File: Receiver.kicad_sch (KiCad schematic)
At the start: 21 parts, among them J15 ReceiverRS485, J23 ReceiverData, U17 AMS1117-5.0, U23 MAX485EE

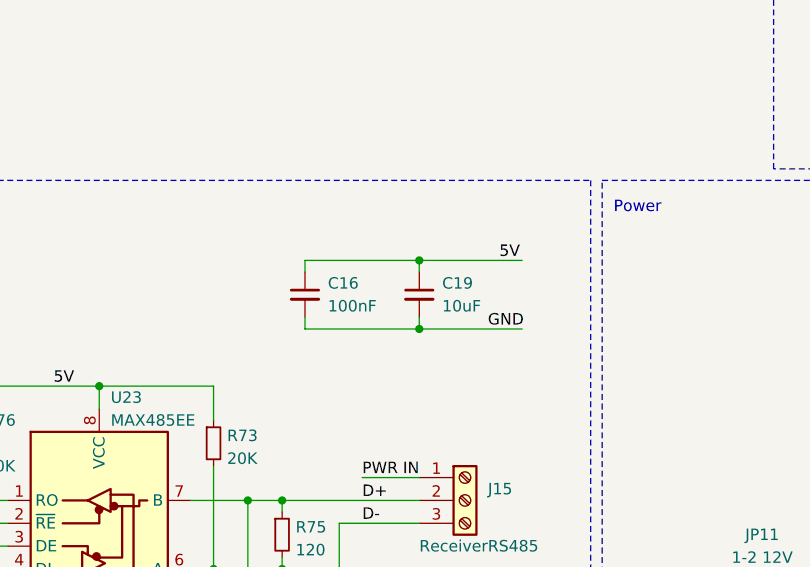
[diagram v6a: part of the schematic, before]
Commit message: fix: DRC & ERC revealed designators were out of sync between schem and pcb
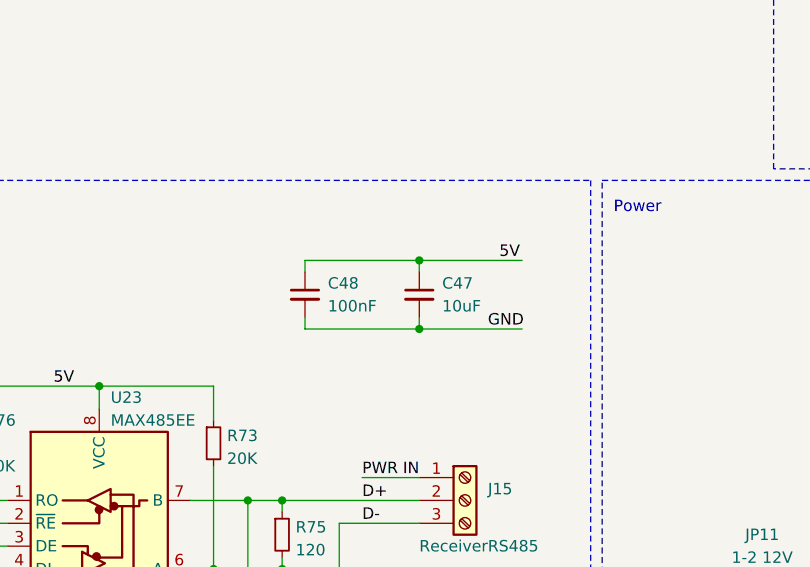
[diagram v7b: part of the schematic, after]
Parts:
- renumbered C19 to C47, C16 to C48
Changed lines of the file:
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@@
   (symbol (lib_id "Device:C_Small") (at 134.62 90.17 0) (unit 1)
     (in_bom yes) (on_board yes) (dnp no) (fields_autoplaced)
-    (property "Reference" "C19" (at 137.16 88.9063 0)
+    (property "Reference" "C47" (at 137.16 88.9063 0)
       (effects (font (size 1.27 1.27)) (justify left))
     )
@@
       (project "rp2040-led-board-schematics-v02"
         (path "/c1a38541-3f06-4b3b-ba3a-decae3ac3c31/757d6d50-47c9-4cb1-8547-9b2447e826a6"
+          (reference "C47") (unit 1)
+        )
+        (path "/c1a38541-3f06-4b3b-ba3a-decae3ac3c31/c0d607bf-2e76-4853-b2ed-907dd6c894fe"
           (reference "C19") (unit 1)
         )
-        (path "/c1a38541-3f06-4b3b-ba3a-decae3ac3c31/c0d607bf-2e76-4853-b2ed-907dd6c894fe"
+        (path "/c1a38541-3f06-4b3b-ba3a-decae3ac3c31/45693edd-6dc6-41b8-8b1c-a9a8e5afcadf"
+          (reference "C50") (unit 1)
+        )
+        (path "/c1a38541-3f06-4b3b-ba3a-decae3ac3c31/50d6fe7a-2d25-4b6a-8e40-e76ae84b788d"
           (reference "C21") (unit 1)
         )
-        (path "/c1a38541-3f06-4b3b-ba3a-decae3ac3c31/45693edd-6dc6-41b8-8b1c-a9a8e5afcadf"
-          (reference "C23") (unit 1)
-        )
-        (path "/c1a38541-3f06-4b3b-ba3a-decae3ac3c31/50d6fe7a-2d25-4b6a-8e40-e76ae84b788d"
+        (path "/c1a38541-3f06-4b3b-ba3a-decae3ac3c31/62e0dde2-ad5d-4205-a74c-f24b413f3931"
+          (reference "C52") (unit 1)
+        )
+        (path "/c1a38541-3f06-4b3b-ba3a-decae3ac3c31/25bef58f-ca62-4f18-ad32-cc60a54b91e0"
+          (reference "C24") (unit 1)
+        )
+        (path "/c1a38541-3f06-4b3b-ba3a-decae3ac3c31/507a174b-d652-466e-bcdb-3655449e938c"
+          (reference "C53") (unit 1)
+        )
+        (path "/c1a38541-3f06-4b3b-ba3a-decae3ac3c31/ceb5b469-5e62-41bb-a8f0-8c2a1861cc28"
           (reference "C25") (unit 1)
-        )
-        (path "/c1a38541-3f06-4b3b-ba3a-decae3ac3c31/62e0dde2-ad5d-4205-a74c-f24b413f3931"
-          (reference "C47") (unit 1)
-        )
-        (path "/c1a38541-3f06-4b3b-ba3a-decae3ac3c31/25bef58f-ca62-4f18-ad32-cc60a54b91e0"
-          (reference "C49") (unit 1)
-        )
-        (path "/c1a38541-3f06-4b3b-ba3a-decae3ac3c31/507a174b-d652-466e-bcdb-3655449e938c"
-          (reference "C51") (unit 1)
-        )
-        (path "/c1a38541-3f06-4b3b-ba3a-decae3ac3c31/ceb5b469-5e62-41bb-a8f0-8c2a1861cc28"
-          (reference "C53") (unit 1)
         )
       )
@@
   (symbol (lib_id "Device:C_Small") (at 121.92 90.17 0) (unit 1)
     (in_bom yes) (on_board yes) (dnp no) (fields_autoplaced)
-    (property "Reference" "C16" (at 124.46 88.9063 0)
+    (property "Reference" "C48" (at 124.46 88.9063 0)
       (effects (font (size 1.27 1.27)) (justify left))
     )
@@
       (project "rp2040-led-board-schematics-v02"
         (path "/c1a38541-3f06-4b3b-ba3a-decae3ac3c31/757d6d50-47c9-4cb1-8547-9b2447e826a6"
-          (reference "C16") (unit 1)
+          (reference "C48") (unit 1)
         )
         (path "/c1a38541-3f06-4b3b-ba3a-decae3ac3c31/c0d607bf-2e76-4853-b2ed-907dd6c894fe"
@@
         )
         (path "/c1a38541-3f06-4b3b-ba3a-decae3ac3c31/45693edd-6dc6-41b8-8b1c-a9a8e5afcadf"
+          (reference "C49") (unit 1)
+        )
+        (path "/c1a38541-3f06-4b3b-ba3a-decae3ac3c31/50d6fe7a-2d25-4b6a-8e40-e76ae84b788d"
           (reference "C22") (unit 1)
         )
-        (path "/c1a38541-3f06-4b3b-ba3a-decae3ac3c31/50d6fe7a-2d25-4b6a-8e40-e76ae84b788d"
-          (reference "C24") (unit 1)
-        )
-        (path "/c1a38541-3f06-4b3b-ba3a-decae3ac3c31/62e0dde2-ad5d-4205-a74c-f24b413f3931"
+        (path "/c1a38541-3f06-4b3b-ba3a-decae3ac3c31/62e0dde2-ad5d-4205-a74c-f24b413f3931"
+          (reference "C51") (unit 1)
+        )
+        (path "/c1a38541-3f06-4b3b-ba3a-decae3ac3c31/25bef58f-ca62-4f18-ad32-cc60a54b91e0"
+          (reference "C23") (unit 1)
+        )
+        (path "/c1a38541-3f06-4b3b-ba3a-decae3ac3c31/507a174b-d652-466e-bcdb-3655449e938c"
+          (reference "C54") (unit 1)
+        )
+        (path "/c1a38541-3f06-4b3b-ba3a-decae3ac3c31/ceb5b469-5e62-41bb-a8f0-8c2a1861cc28"
           (reference "C26") (unit 1)
         )
-        (path "/c1a38541-3f06-4b3b-ba3a-decae3ac3c31/25bef58f-ca62-4f18-ad32-cc60a54b91e0"
-          (reference "C48") (unit 1)
-        )
-        (path "/c1a38541-3f06-4b3b-ba3a-decae3ac3c31/507a174b-d652-466e-bcdb-3655449e938c"
-          (reference "C50") (unit 1)
-        )
-        (path "/c1a38541-3f06-4b3b-ba3a-decae3ac3c31/ceb5b469-5e62-41bb-a8f0-8c2a1861cc28"
-          (reference "C52") (unit 1)
-        )
-      )
+      )

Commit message: order placed
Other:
- note added: "current draw: ~10mA"
- note removed: "current draw: ~50mA"
- moved on the sheet: C29, C38, C55, C63, JP11, JP15, U17
